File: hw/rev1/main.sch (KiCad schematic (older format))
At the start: 28 parts, among them J10 NSM E-004 Counter power/speed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, J11 NSM E-004 Counter power & RS4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, J4 POWER, J6 AVR-ISP-6, J7 NSM E-004 Controller RS485, J8 UART, J9 Speed/reverse, U3 ATmega168-20AU, U4 ADM485AR, Y1 16MHz

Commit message: В схему добавлен забытый ZCD.
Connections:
- net at J9.1 (Pin_1), R53.1: no longer J10.1 (Pin_1)
- net at J9.3 (Pin_3), R54.1: now also J10.1 (Pin_1)
- net analog section/ZCD: now reaches U3.25 (PC2)
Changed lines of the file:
@@
 $EndComp
 Wire Wire Line
-	8500 1500 8750 1500
-Wire Wire Line
-	8500 1700 9050 1700
+	8500 1700 8750 1700
 $Comp
 L Device:Jumper TP1
@@
 Wire Wire Line
 	9050 1050 8750 1050
-Wire Wire Line
-	8750 1050 8750 1500
-Connection ~ 8750 1500
-Wire Wire Line
-	8750 1500 9050 1500
 $Sheet
 S 3250 3200 850  300
@@
 F3 "PWM" I L 3250 3400 50
 F4 "Reverse" I L 3250 3300 50
+F5 "ZCD" O R 4100 3400 50
 $EndSheet
 Wire Wire Line
@@
 	1    0    0    -1
 $EndComp
+Wire Wire Line
+	2650 2500 3250 2500
+Wire Wire Line
+	3250 2500 3250 3000
+Wire Wire Line
+	3250 3000 4300 3000
+Wire Wire Line
+	4300 3000 4300 3400
+Wire Wire Line
+	4300 3400 4100 3400
+Connection ~ 8750 1700
+Wire Wire Line
+	8750 1700 9050 1700
+Wire Wire Line
+	8500 1500 9050 1500
+Wire Wire Line
+	8750 1050 8750 1700
 $EndSCHEMATC

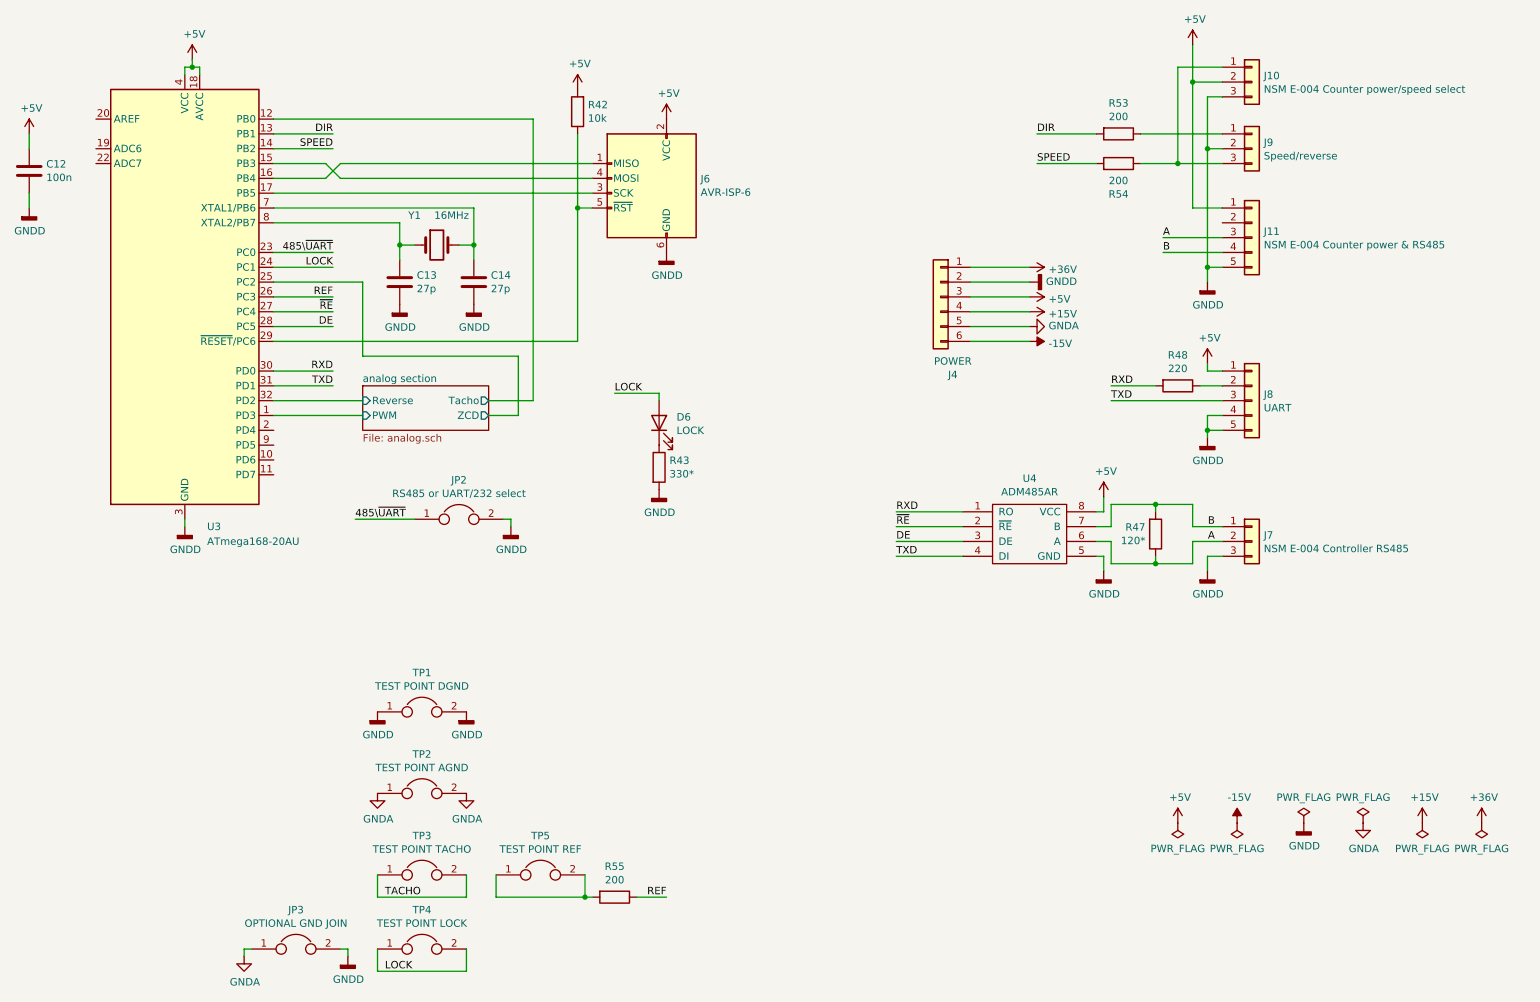
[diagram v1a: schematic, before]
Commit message: Добавлена печатная плата rev1 (вероятно чистовая).
+ Обозначена и разведена схема ZCD;
+ Исключена схема аналогового перемножителя;
  * модуляция модулем синуса полностью цифровая;
+ LM324 использована полностью:
  * собран 2й PWM фильтр, подключенный к OC2A в отладочных целях;
+ Добавлен доп. светодиод, предназначенный для контроля за ZCD;
+ Исправлен разъем логических сигналов управления;
+ Всякие незначимые украшательства.
+ Немного документирована плата rev0.
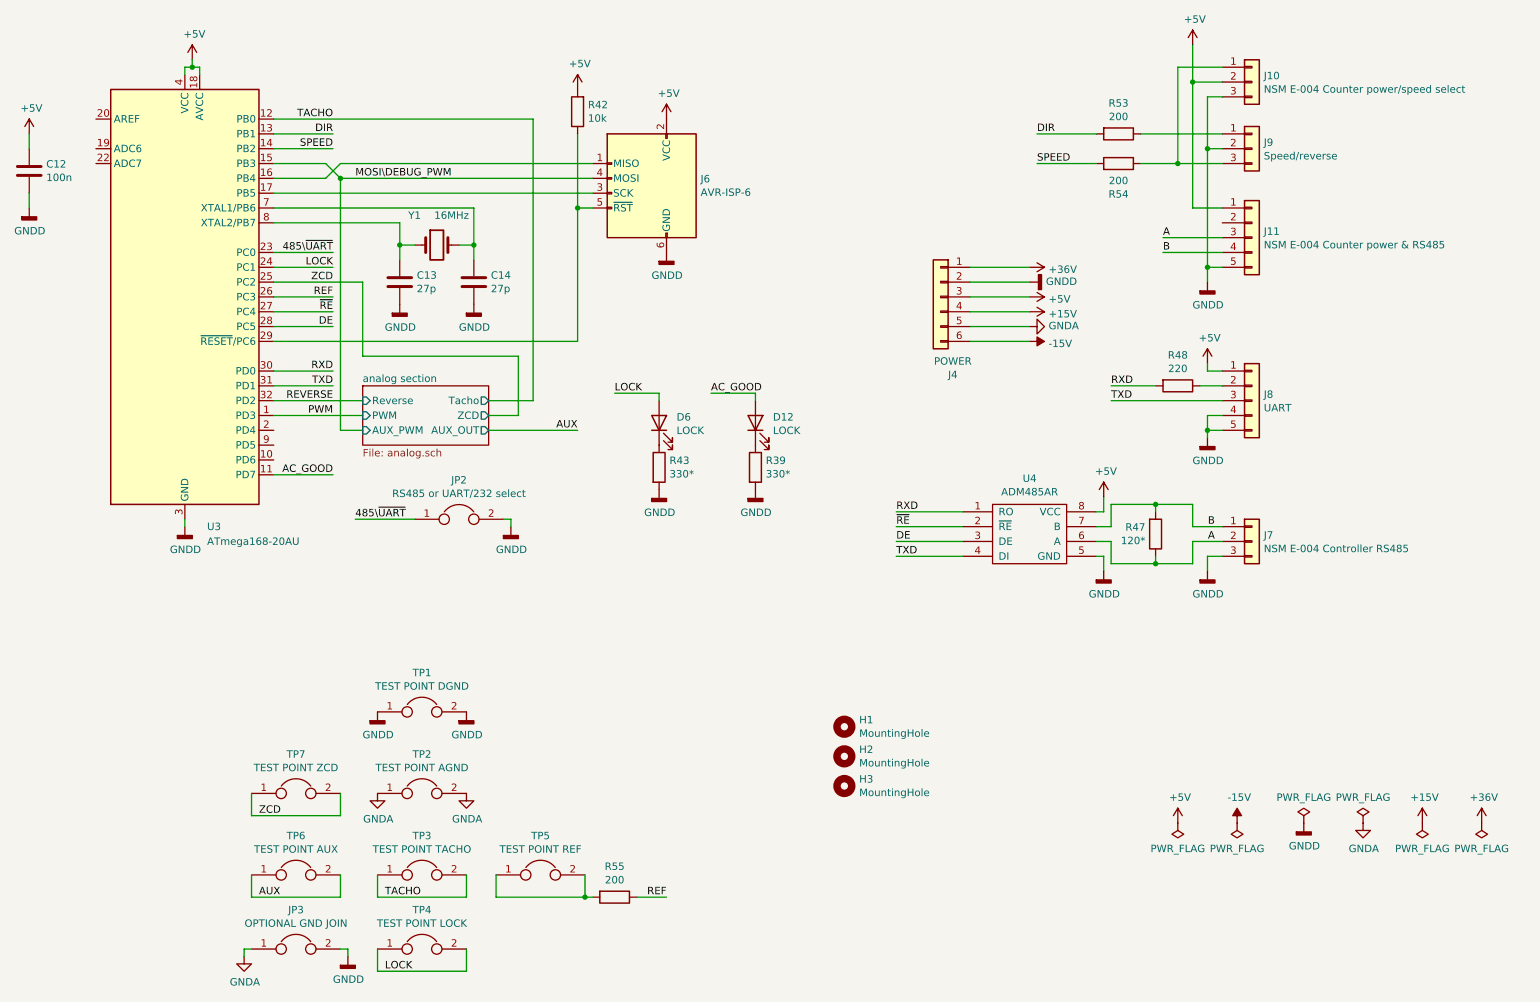
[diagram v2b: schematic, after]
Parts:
- added D12: LOCK, LED_SMD:LED_0805_2012Metric, symbol Device:LED
- added H1, H2, H3: MountingHole, MountingHole:MountingHole_3.2mm_M3, symbol Mechanical:MountingHole
- added R39: 330*, Resistor_SMD:R_0805_2012Metric, symbol Device:R
- added TP6: TEST POINT AUX, Connector_PinHeader_2.54mm:PinHeader_2x01_P2.54mm_Vertical, symbol Device:Jumper
- added TP7: TEST POINT ZCD, Connector_PinHeader_2.54mm:PinHeader_2x01_P2.54mm_Vertical, symbol Device:Jumper
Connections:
- net analog section/Tacho is gone; now on net TACHO: U3.12 (PB0)
- net GNDD: now also R39.2
- net MOSI\DEBUG_PWM: now reaches J6.4 (MOSI), U3.15 (PB3)
- net AC_GOOD: now reaches U3.11 (PD7)
- net AC_GOOD: now also D12.2 (A)
- net analog section/PWM renamed PWM
- net analog section/Reverse renamed REVERSE
- net analog section/ZCD renamed ZCD
- net ZCD: now also TP7.1, TP7.2
- new net: D12.1 (K), R39.1
- new net AUX: TP6.1, TP6.2
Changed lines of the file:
@@
 	2650 1900 4800 1900
-Wire Wire Line
-	4800 1800 3100 1800
 Wire Wire Line
 	3100 1800 3000 1700
@@
 	9050 1050 8750 1050
 $Sheet
-S 3250 3200 850  300
+S 3250 3200 850  400
 U 61F382E3
 F0 "analog section" 50
@@
 F4 "Reverse" I L 3250 3300 50
 F5 "ZCD" O R 4100 3400 50
+F6 "AUX_PWM" I L 3250 3500 50
+F7 "AUX_OUT" O R 4100 3500 50
 $EndSheet
 Wire Wire Line
@@
 	2650 1400 4400 1400
 $Comp
-L power:+36V #PWR?
+L power:+36V #PWR01
 U 1 1 62246AF8
 P 7750 2400
-F 0 "#PWR?" H 7750 2250 50  0001 C CNN
+F 0 "#PWR01" H 7750 2250 50  0001 C CNN
 F 1 "+36V" V 7765 2528 50  0000 L CNN
 F 2 "" H 7750 2400 50  0001 C CNN
@@
 $EndComp
 $Comp
-L power:GNDD #PWR?
+L power:GNDD #PWR02
 U 1 1 622566E7
 P 7750 2500
-F 0 "#PWR?" H 7750 2250 50  0001 C CNN
+F 0 "#PWR02" H 7750 2250 50  0001 C CNN
 F 1 "GNDD" V 7754 2390 50  0000 R CNN
 F 2 "" H 7750 2500 50  0001 C CNN
@@
 $EndComp
 $Comp
-L power:+15V #PWR?
+L power:+15V #PWR04
 U 1 1 6227E062
 P 7750 2700
-F 0 "#PWR?" H 7750 2550 50  0001 C CNN
+F 0 "#PWR04" H 7750 2550 50  0001 C CNN
 F 1 "+15V" V 7765 2828 50  0000 L CNN
 F 2 "" H 7750 2700 50  0001 C CNN
@@
 $EndComp
 $Comp
-L power:-15V #PWR?
+L power:-15V #PWR06
 U 1 1 6227EF3D
 P 7750 2900
-F 0 "#PWR?" H 7750 3000 50  0001 C CNN
+F 0 "#PWR06" H 7750 3000 50  0001 C CNN
 F 1 "-15V" V 7765 3028 50  0000 L CNN
 F 2 "" H 7750 2900 50  0001 C CNN
@@
 $EndComp
 $Comp
-L power:GNDA #PWR?
+L power:GNDA #PWR05
 U 1 1 62288661
 P 7750 2800
-F 0 "#PWR?" H 7750 2550 50  0001 C CNN
+F 0 "#PWR05" H 7750 2550 50  0001 C CNN
 F 1 "GNDA" V 7755 2672 50  0000 R CNN
 F 2 "" H 7750 2800 50  0001 C CNN
@@
 	7750 2700 7350 2700
 $Comp
-L power:+5V #PWR?
+L power:+5V #PWR03
 U 1 1 622D5EFF
 P 7750 2600
-F 0 "#PWR?" H 7750 2450 50  0001 C CNN
+F 0 "#PWR03" H 7750 2450 50  0001 C CNN
 F 1 "+5V" V 7765 2728 50  0000 L CNN
 F 2 "" H 7750 2600 50  0001 C CNN
@@
 P 8750 6150
 AR Path="/61F382E3/6231086A" Ref="#PWR?"  Part="1"
-AR Path="/6231086A" Ref="#PWR?"  Part="1"
-F 0 "#PWR?" H 8750 6000 50  0001 C CNN
+AR Path="/6231086A" Ref="#PWR07"  Part="1"
+F 0 "#PWR07" H 8750 6000 50  0001 C CNN
 F 1 "+5V" H 8765 6323 50  0000 C CNN
 F 2 "" H 8750 6150 50  0001 C CNN
@@
 P 8750 6150
 AR Path="/61F382E3/62310870" Ref="#FLG?"  Part="1"
-AR Path="/62310870" Ref="#FLG?"  Part="1"
-F 0 "#FLG?" H 8750 6225 50  0001 C CNN
+AR Path="/62310870" Ref="#FLG01"  Part="1"
+F 0 "#FLG01" H 8750 6225 50  0001 C CNN
 F 1 "PWR_FLAG" H 8750 6323 50  0000 C CNN
 F 2 "" H 8750 6150 50  0001 C CNN
@@
 P 10400 6150
 AR Path="/61F382E3/62310876" Ref="#PWR?"  Part="1"
-AR Path="/62310876" Ref="#PWR?"  Part="1"
-F 0 "#PWR?" H 10400 6000 50  0001 C CNN
+AR Path="/62310876" Ref="#PWR011"  Part="1"
+F 0 "#PWR011" H 10400 6000 50  0001 C CNN
 F 1 "+15V" H 10415 6323 50  0000 C CNN
 F 2 "" H 10400 6150 50  0001 C CNN
@@
 P 9150 6150
 AR Path="/61F382E3/6231087C" Ref="#PWR?"  Part="1"
-AR Path="/6231087C" Ref="#PWR?"  Part="1"
-F 0 "#PWR?" H 9150 6250 50  0001 C CNN
+AR Path="/6231087C" Ref="#PWR08"  Part="1"
+F 0 "#PWR08" H 9150 6250 50  0001 C CNN
 F 1 "-15V" H 9165 6323 50  0000 C CNN
 F 2 "" H 9150 6150 50  0001 C CNN
@@
 P 10400 6150
 AR Path="/61F382E3/62310882" Ref="#FLG?"  Part="1"
-AR Path="/62310882" Ref="#FLG?"  Part="1"
-F 0 "#FLG?" H 10400 6225 50  0001 C CNN
+AR Path="/62310882" Ref="#FLG05"  Part="1"
+F 0 "#FLG05" H 10400 6225 50  0001 C CNN
 F 1 "PWR_FLAG" H 10400 6323 50  0000 C CNN
 F 2 "" H 10400 6150 50  0001 C CNN
@@
 P 10000 6150
 AR Path="/61F382E3/62310888" Ref="#PWR?"  Part="1"
-AR Path="/62310888" Ref="#PWR?"  Part="1"
-F 0 "#PWR?" H 10000 5900 50  0001 C CNN
+AR Path="/62310888" Ref="#PWR010"  Part="1"
+F 0 "#PWR010" H 10000 5900 50  0001 C CNN
 F 1 "GNDA" H 10005 5977 50  0000 C CNN
 F 2 "" H 10000 6150 50  0001 C CNN
@@
 P 10000 6150
 AR Path="/61F382E3/6231088E" Ref="#FLG?"  Part="1"
-AR Path="/6231088E" Ref="#FLG?"  Part="1"
-F 0 "#FLG?" H 10000 6225 50  0001 C CNN
+AR Path="/6231088E" Ref="#FLG04"  Part="1"
+F 0 "#FLG04" H 10000 6225 50  0001 C CNN
 F 1 "PWR_FLAG" H 10000 6323 50  0000 C CNN
 F 2 "" H 10000 6150 50  0001 C CNN
@@
 P 9150 6150
 AR Path="/61F382E3/62310894" Ref="#FLG?"  Part="1"
-AR Path="/62310894" Ref="#FLG?"  Part="1"
-F 0 "#FLG?" H 9150 6225 50  0001 C CNN
+AR Path="/62310894" Ref="#FLG02"  Part="1"
+F 0 "#FLG02" H 9150 6225 50  0001 C CNN
 F 1 "PWR_FLAG" H 9150 6323 50  0000 C CNN
 F 2 "" H 9150 6150 50  0001 C CNN
@@
 P 9600 6150
 AR Path="/61F382E3/6231089A" Ref="#FLG?"  Part="1"
-AR Path="/6231089A" Ref="#FLG?"  Part="1"
-F 0 "#FLG?" H 9600 6225 50  0001 C CNN
+AR Path="/6231089A" Ref="#FLG03"  Part="1"
+F 0 "#FLG03" H 9600 6225 50  0001 C CNN
 F 1 "PWR_FLAG" H 9600 6323 50  0000 C CNN
 F 2 "" H 9600 6150 50  0001 C CNN
@@
 P 9600 6150
 AR Path="/61F382E3/623108A0" Ref="#PWR?"  Part="1"
-AR Path="/623108A0" Ref="#PWR?"  Part="1"
-F 0 "#PWR?" H 9600 5900 50  0001 C CNN
+AR Path="/623108A0" Ref="#PWR09"  Part="1"
+F 0 "#PWR09" H 9600 5900 50  0001 C CNN
 F 1 "GNDD" H 9604 5995 50  0000 C CNN
 F 2 "" H 9600 6150 50  0001 C CNN
@@
 P 10800 6150
 AR Path="/61F382E3/623108A6" Ref="#FLG?"  Part="1"
-AR Path="/623108A6" Ref="#FLG?"  Part="1"
-F 0 "#FLG?" H 10800 6225 50  0001 C CNN
+AR Path="/623108A6" Ref="#FLG06"  Part="1"
+F 0 "#FLG06" H 10800 6225 50  0001 C CNN
 F 1 "PWR_FLAG" H 10800 6323 50  0000 C CNN
 F 2 "" H 10800 6150 50  0001 C CNN
@@
 P 10800 6150
 AR Path="/61F382E3/623108AC" Ref="#PWR?"  Part="1"
-AR Path="/623108AC" Ref="#PWR?"  Part="1"
-F 0 "#PWR?" H 10800 6000 50  0001 C CNN
+AR Path="/623108AC" Ref="#PWR012"  Part="1"
+F 0 "#PWR012" H 10800 6000 50  0001 C CNN
 F 1 "+36V" H 10815 6323 50  0000 C CNN
 F 2 "" H 10800 6150 50  0001 C CNN
@@
 Wire Wire Line
 	8750 1050 8750 1700
+Text Label 3050 1400 2    50   ~ 0
+TACHO
+Text Label 3050 3400 2    50   ~ 0
+PWM
+Text Label 3050 3300 2    50   ~ 0
+REVERSE
+Text Label 3200 1800 0    50   ~ 0
+MOSI\DEBUG_PWM
+$Comp
+L Device:Jumper TP6
+U 1 1 6234069C
+P 2800 6500
+F 0 "TP6" H 2800 6764 50  0000 C CNN
+F 1 "TEST POINT AUX" H 2800 6673 50  0000 C CNN
+F 2 "Connector_PinHeader_2.54mm:PinHeader_2x01_P2.54mm_Vertical" H 2800 6500 50  0001 C CNN
+F 3 "~" H 2800 6500 50  0001 C CNN
+	1    2800 6500
+	1    0    0    -1
+$EndComp
+Wire Wire Line
+	2500 6500 2500 6650
+Wire Wire Line
+	2500 6650 3100 6650
+Text Label 2550 6650 0    50   ~ 0
+AUX
+Wire Wire Line
+	3100 6650 3100 6500
+Wire Wire Line
+	4800 1800 3100 1800
+Wire Wire Line
+	3250 3500 3100 3500
+Wire Wire Line
+	3100 3500 3100 1800
+Connection ~ 3100 1800
+Wire Wire Line
+	4100 3500 4700 3500
+Text Label 4700 3500 2    50   ~ 0
+AUX
+$Comp
+L Device:LED D12
+U 1 1 6236ACF1
+P 5900 3450
+F 0 "D12" V 5939 3332 50  0000 R CNN
+F 1 "LOCK" V 5848 3332 50  0000 R CNN
+F 2 "LED_SMD:LED_0805_2012Metric" H 5900 3450 50  0001 C CNN
+F 3 "~" H 5900 3450 50  0001 C CNN
+	1    5900 3450
+	0    -1   -1   0
+$EndComp
+$Comp
+L Device:R R39
+U 1 1 6236AE91
+P 5900 3750
+F 0 "R39" H 5970 3796 50  0000 L CNN
+F 1 "330*" H 5970 3705 50  0000 L CNN
+F 2 "Resistor_SMD:R_0805_2012Metric" V 5830 3750 50  0001 C CNN
+F 3 "~" H 5900 3750 50  0001 C CNN
+	1    5900 3750
+	1    0    0    -1
+$EndComp
+$Comp
+L power:GNDD #PWR0101
+U 1 1 6236AE9B
+P 5900 3900
+F 0 "#PWR0101" H 5900 3650 50  0001 C CNN
+F 1 "GNDD" H 5904 3745 50  0000 C CNN
+F 2 "" H 5900 3900 50  0001 C CNN
+F 3 "" H 5900 3900 50  0001 C CNN
+	1    5900 3900
+	1    0    0    -1
+$EndComp
+Wire Wire Line
+	5900 3300 5900 3250
+Wire Wire Line
+	5900 3250 5600 3250
+Text Label 5600 3250 0    50   ~ 0
+AC_GOOD
+Text Label 3050 3800 2    50   ~ 0
+AC_GOOD
+Wire Wire Line
+	2650 3800 3050 3800
+$Comp
+L Device:Jumper TP7
+U 1 1 62397906
+P 2800 5950
+F 0 "TP7" H 2800 6214 50  0000 C CNN
+F 1 "TEST POINT ZCD" H 2800 6123 50  0000 C CNN
+F 2 "Connector_PinHeader_2.54mm:PinHeader_2x01_P2.54mm_Vertical" H 2800 5950 50  0001 C CNN
+F 3 "~" H 2800 5950 50  0001 C CNN
+	1    2800 5950
+	1    0    0    -1
+$EndComp
+Wire Wire Line
+	2500 5950 2500 6100
+Wire Wire Line
+	2500 6100 3100 6100
+Text Label 2550 6100 0    50   ~ 0
+ZCD
+Wire Wire Line
+	3100 6100 3100 5950
+Text Label 3050 2500 2    50   ~ 0
+ZCD
+$Comp
+L Mechanical:MountingHole H1
+U 1 1 62405EBA
+P 6500 5500
+F 0 "H1" H 6600 5546 50  0000 L CNN
+F 1 "MountingHole" H 6600 5455 50  0000 L CNN
+F 2 "MountingHole:MountingHole_3.2mm_M3" H 6500 5500 50  0001 C CNN
+F 3 "~" H 6500 5500 50  0001 C CNN
+	1    6500 5500
+	1    0    0    -1
+$EndComp
+$Comp
+L Mechanical:MountingHole H2
+U 1 1 62411FEE
+P 6500 5700
+F 0 "H2" H 6600 5746 50  0000 L CNN
+F 1 "MountingHole" H 6600 5655 50  0000 L CNN
+F 2 "MountingHole:MountingHole_3.2mm_M3" H 6500 5700 50  0001 C CNN
+F 3 "~" H 6500 5700 50  0001 C CNN
+	1    6500 5700
+	1    0    0    -1
+$EndComp
+$Comp
+L Mechanical:MountingHole H3
+U 1 1 6241B81D
+P 6500 5900
+F 0 "H3" H 6600 5946 50  0000 L CNN
+F 1 "MountingHole" H 6600 5855 50  0000 L CNN
+F 2 "MountingHole:MountingHole_3.2mm_M3" H 6500 5900 50  0001 C CNN
+F 3 "~" H 6500 5900 50  0001 C CNN
+	1    6500 5900
+	1    0    0    -1
+$EndComp
 $EndSCHEMATC
